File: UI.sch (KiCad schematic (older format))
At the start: 6 parts

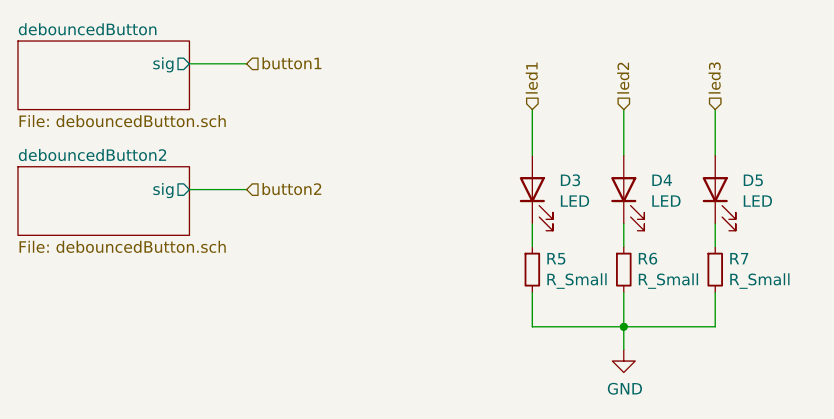
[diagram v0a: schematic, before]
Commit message: rev 1a, XO fixed, more labels and rearranging
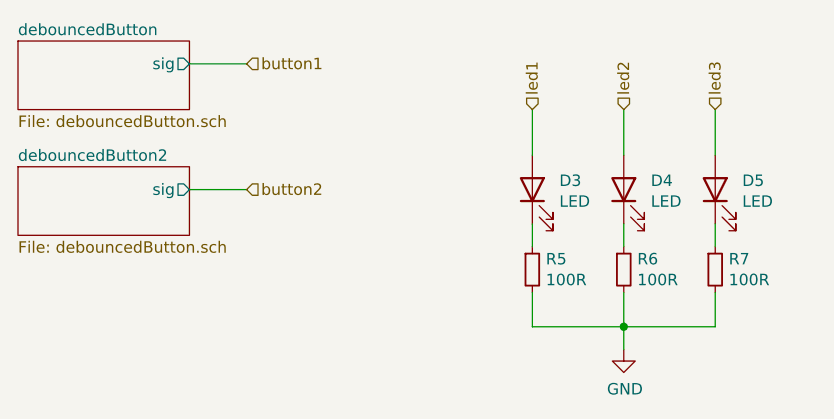
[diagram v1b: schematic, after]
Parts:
- R5, R6, R7: value R_Small -> 100R
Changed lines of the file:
@@
 P 5250 3000
 F 0 "R5" H 5309 3046 50  0000 L CNN
-F 1 "R_Small" H 5309 2955 50  0000 L CNN
+F 1 "100R" H 5309 2955 50  0000 L CNN
 F 2 "Resistor_SMD:R_0603_1608Metric" H 5250 3000 50  0001 C CNN
 F 3 "~" H 5250 3000 50  0001 C CNN
@@
 P 5650 3000
 F 0 "R6" H 5709 3046 50  0000 L CNN
-F 1 "R_Small" H 5709 2955 50  0000 L CNN
+F 1 "100R" H 5709 2955 50  0000 L CNN
 F 2 "Resistor_SMD:R_0603_1608Metric" H 5650 3000 50  0001 C CNN
 F 3 "~" H 5650 3000 50  0001 C CNN
@@
 P 6050 3000
 F 0 "R7" H 6109 3046 50  0000 L CNN
-F 1 "R_Small" H 6109 2955 50  0000 L CNN
+F 1 "100R" H 6109 2955 50  0000 L CNN
 F 2 "Resistor_SMD:R_0603_1608Metric" H 6050 3000 50  0001 C CNN
 F 3 "~" H 6050 3000 50  0001 C CNN
